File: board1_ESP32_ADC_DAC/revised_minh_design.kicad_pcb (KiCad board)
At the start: 4 copper layers, 94 x 39 mm, 31 parts, among them J1 Conn_01x03_Male, J2 Conn_01x08_Male, J3 Conn_01x08_Male, J4 Conn_01x08_Male, U1 ESP32-DevKit-C, U2 LM7805_TO220, U3 MCP1754S-3302xCB, U4 MCP1825S-3.3V, U5 MCP1501-33xSN, U6 MCP3464R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

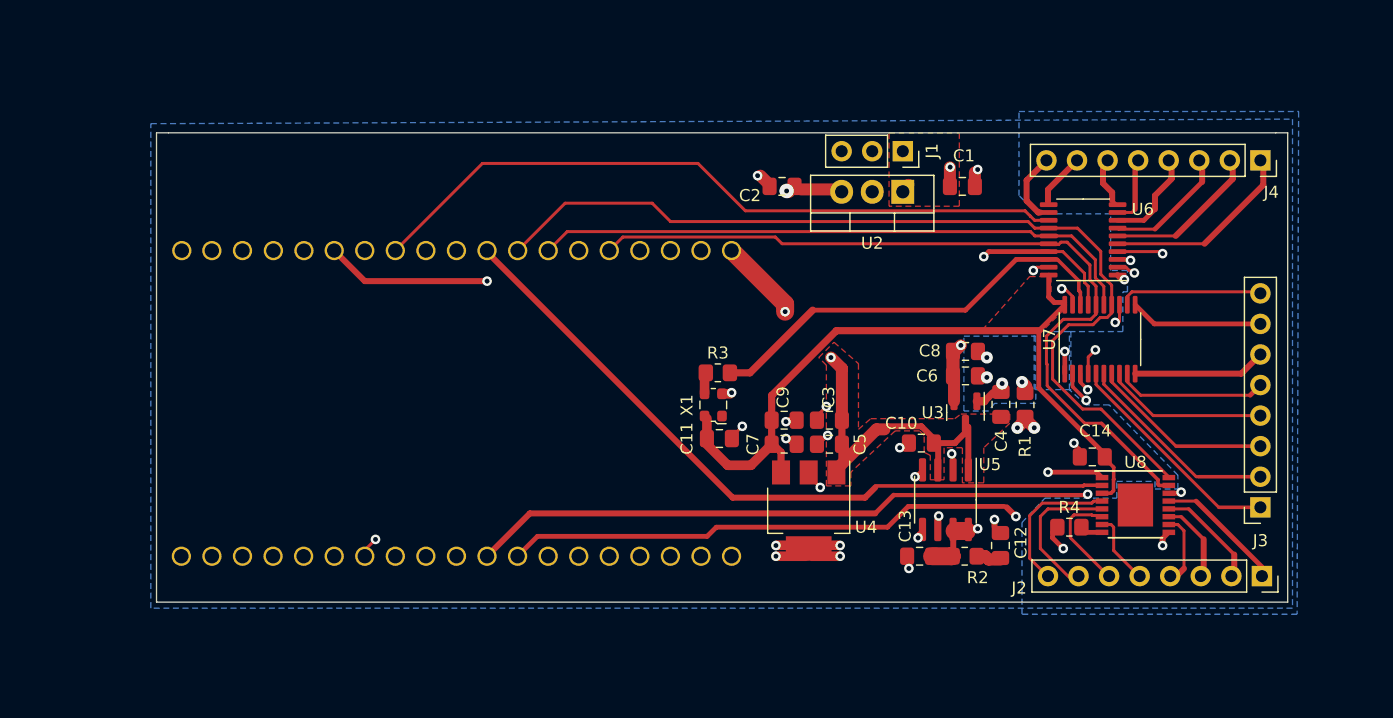
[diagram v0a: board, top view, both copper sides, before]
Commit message: Fab ready version with joined ground plane, extra caps for ADCs
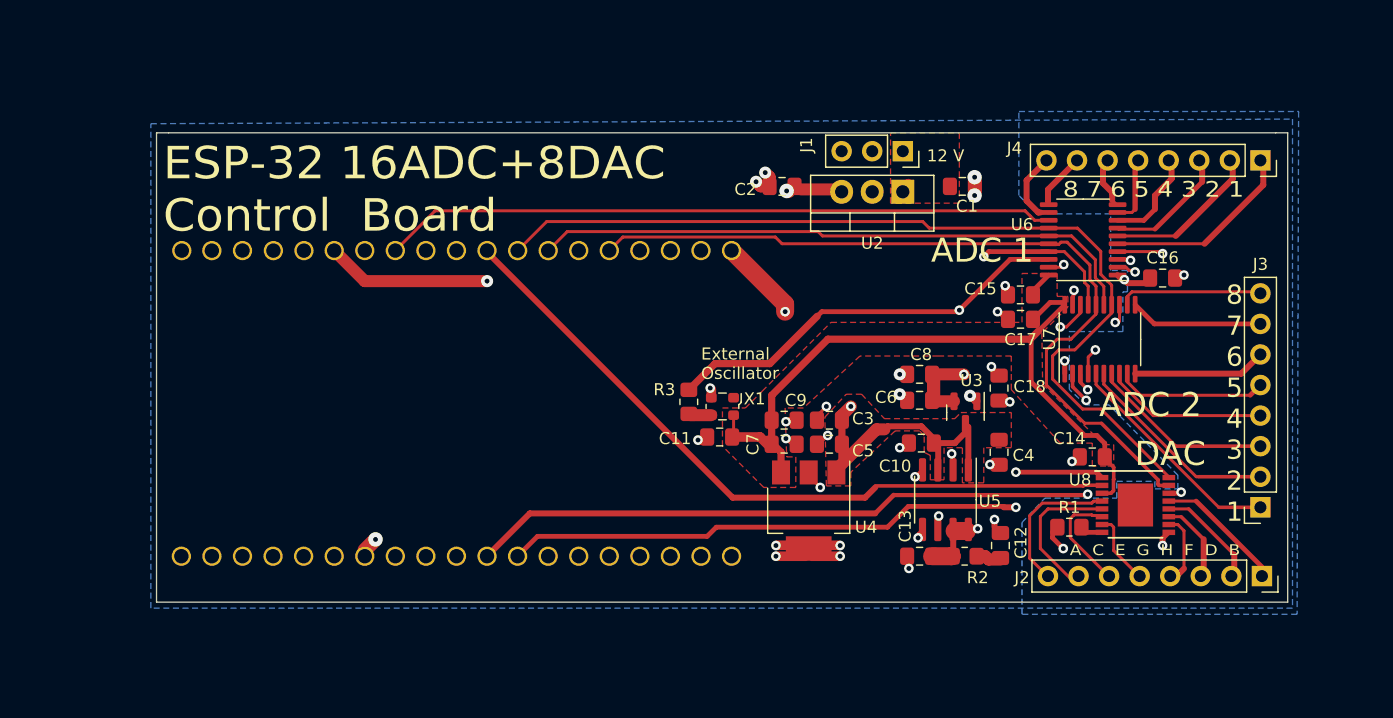
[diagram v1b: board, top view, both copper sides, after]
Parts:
- removed the R1 at (122.2, 62.6)
- added C15: 0.1uF, Capacitor_SMD:C_0805_2012Metric_Pad1.18x1.45mm_HandSolder, F.Cu at (121.8, 53.5)
- added C16: 0.1uF, Capacitor_SMD:C_0805_2012Metric_Pad1.18x1.45mm_HandSolder, F.Cu at (133.6, 52.1)
- added C17: 0.1uF, Capacitor_SMD:C_0805_2012Metric_Pad1.18x1.45mm_HandSolder, F.Cu at (121.8, 55.5)
- added C18: 0.1uF, Capacitor_SMD:C_0805_2012Metric_Pad1.18x1.45mm_HandSolder, F.Cu at (120.0, 61.2)
- moved C6 4.32 mm to (113.4, 62.2), turned to 180 degrees
- moved C8 4.26 mm to (113.4, 60.1), turned to 180 degrees
- moved C4 3.98 mm to (120.0, 66.5), turned to -90 degrees
- moved R3 3.41 mm to (94.2, 62.4), turned to 90 degrees
- moved X1 0.77 mm to (97.0, 62.7), turned to -90 degrees
- moved C11 0.13 mm to (96.8, 65.3), turned to 180 degrees
- renumbered R4 to R1
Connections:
- C4 pad 2: GNDA -> Earth
- C6 pad 2: GNDA -> Earth
- C8 pad 2: GNDA -> Earth
- U3 pad 1: GNDA -> Earth
- U6 pad 2: GNDA -> Earth
- U6 pad 3: GNDA -> Earth
- U7 pad 2: GNDA -> Earth
- U7 pad 3: GNDA -> Earth
- U8 pad 14: GNDA -> Earth
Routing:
- net GNDA: track 13.0 -> 0.00 mm, vias 9 -> 0
- net CLK: track 35.7 -> 46.6 mm, vias 0 -> 2
- net Earth: track 39.9 -> 47.8 mm, vias 26 -> 39
- net +3.3VA: track 27.2 -> 31.0 mm, vias 3 -> 4
- net ~{ADC1_CS}: track 59.2 -> 56.0 mm
- net SK: track 79.4 -> 77.4 mm
- net +12V: track 2.76 -> 1.28 mm, vias 1 -> 0
- net +5V: track 54.5 -> 53.3 mm
- net +3V3: track 63.0 -> 61.8 mm
- net LDAC: track 52.7 -> 53.4 mm
- net SO: track 68.6 -> 67.9 mm
- removed copper zone on B.Cu, net GNDA
- removed copper zone on In1.Cu, net GNDA
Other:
- board text added: "12 V"
- board text added: "8 7 6 5 4 3 2 1"
- board text added: "A C E G H F D B"
- board text added: "ADC 1"
- board text added: "ADC 2"
- board text added: "Antenna this way ->"
- board text added: "DAC"
- board text added: "ESP-32 16ADC+8DAC Control Board"
- board text added: "ESP-32 Here"
- board text added: "External Oscillator"

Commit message: Repositioned clock closer
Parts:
- moved R3 23.5 mm to (116.1, 53.7), turned to -90 degrees
- moved X1 18.5 mm to (113.4, 54.2), turned to 90 degrees
- moved C11 17.0 mm to (110.2, 54.9), turned to 90 degrees
- moved C14 0.87 mm to (126.9, 66.9)
- moved C12 0.25 mm to (120.1, 74.5)
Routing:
- net CLK: track 46.6 -> 21.6 mm
- net +3V3: track 61.8 -> 59.8 mm
- net +3.3VDAC: track 50.8 -> 49.8 mm
- added copper zone on F.Cu, net +3.3VDAC

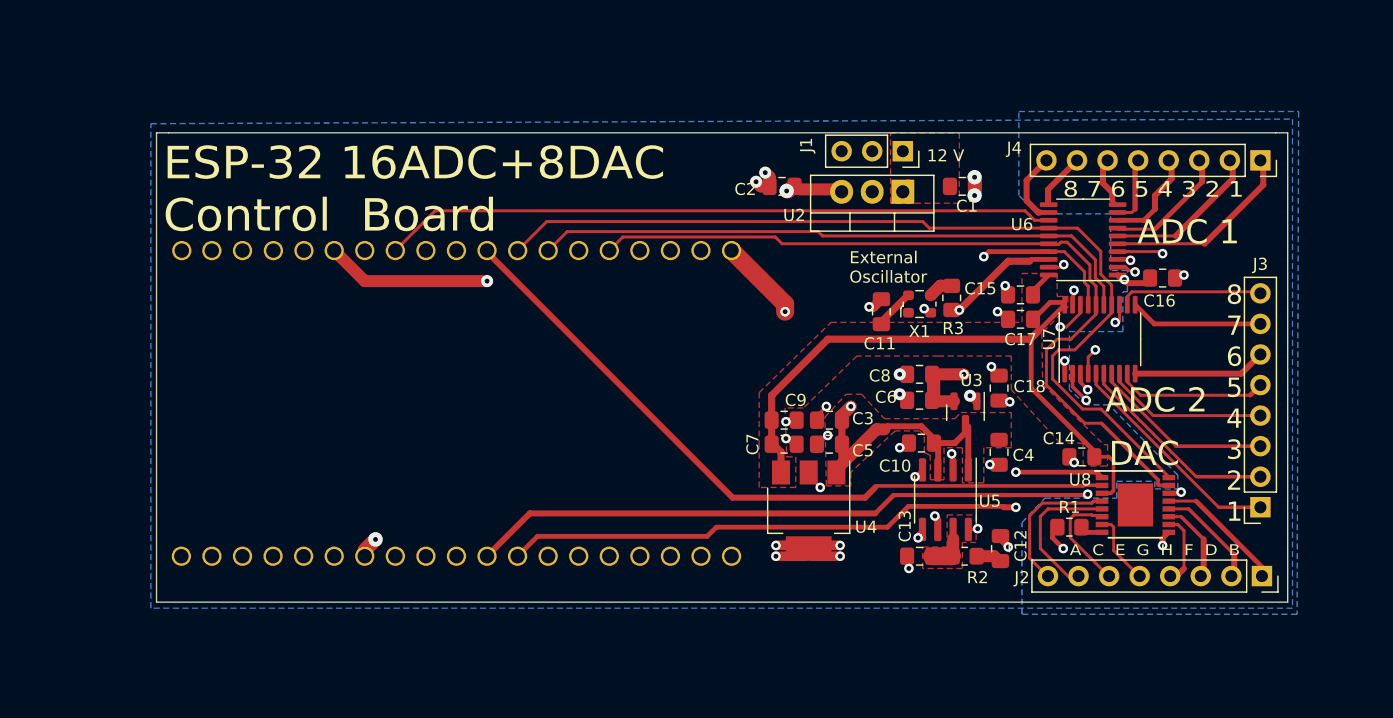
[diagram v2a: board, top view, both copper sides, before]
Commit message: JLCPB Submission. Name added, connectors changed to double layer
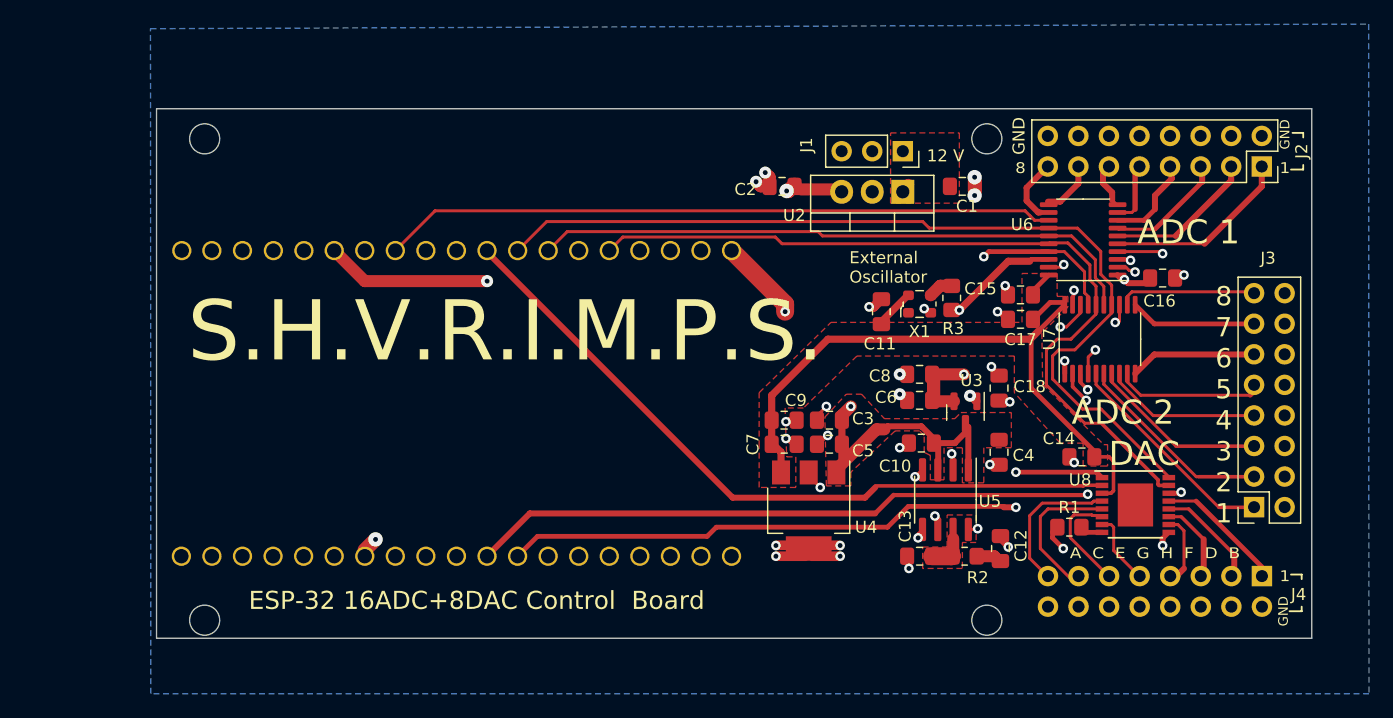
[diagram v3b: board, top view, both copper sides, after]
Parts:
- added  : MountingHole_2.5mm, MountingHole:MountingHole_2.5mm, F.Cu at (54.0, 40.5)
- added  : MountingHole_2.5mm, MountingHole:MountingHole_2.5mm, F.Cu at (119.0, 40.5)
- added  : MountingHole_2.5mm, MountingHole:MountingHole_2.5mm, F.Cu at (119.0, 80.5)
- added  : MountingHole_2.5mm, MountingHole:MountingHole_2.5mm, F.Cu at (54.0, 80.5)
- J2, J3: value Conn_01x08_Male -> Conn_02x08_Odd_Even; footprint Connector_PinSocket_2.54mm:PinSocket_1x08_P2.54mm_Vertical -> Connector_PinSocket_2.54mm:PinSocket_2x08_P2.54mm_Vertical
- J4: value Conn_01x08_Male -> Conn_02x08_Odd_Even; footprint Connector_PinSocket_2.54mm:PinSocket_1x08_P2.54mm_Vertical -> Connector_PinSocket_2.54mm:PinSocket_2x08_P2.54mm_Vertical; moved to B.Cu
- moved J4 34.5 mm to (141.9, 76.8), turned to 90 degrees
- moved J2 34.0 mm to (141.8, 42.8)
- moved J3 0.53 mm to (141.2, 71.1)
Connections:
- J2 pad 1: VoutB -> ADC1_1
- J2 pad 2: VoutD -> Earth
- J2 pad 3: VoutF -> ADC1_2
- J2 pad 4: VoutH -> Earth
- J2 pad 5: VoutG -> ADC1_3
- J2 pad 6: VoutE -> Earth
- J2 pad 7: VoutC -> ADC1_4
- J2 pad 8: VoutA -> Earth
- J3 pad 2: ADC2_2 -> Earth
- J3 pad 3: ADC2_3 -> ADC2_2
- J3 pad 4: ADC2_4 -> Earth
- J3 pad 5: ADC2_5 -> ADC2_3
- J3 pad 6: ADC2_6 -> Earth
- J3 pad 7: ADC2_7 -> ADC2_4
- J3 pad 8: ADC2_8 -> Earth
- J4 pad 1: ADC1_1 -> VoutB
- J4 pad 2: ADC1_2 -> Earth
- J4 pad 3: ADC1_3 -> VoutD
- J4 pad 4: ADC1_4 -> Earth
- J4 pad 5: ADC1_5 -> VoutF
- J4 pad 6: ADC1_6 -> Earth
- J4 pad 7: ADC1_7 -> VoutH
- J4 pad 8: ADC1_8 -> Earth
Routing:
- net ADC1_1: track 16.4 -> 15.6 mm
- net ADC1_8: track 6.61 -> 5.82 mm
- net ADC1_2: track 13.3 -> 12.5 mm
- net ADC1_4: track 8.36 -> 7.66 mm
- net ADC1_5: track 6.06 -> 5.37 mm
- net ADC1_3: track 10.7 -> 10.0 mm
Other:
- board size 94 x 39 mm -> 96 x 44 mm
- board text added: "1"
- board text added: "8"
- board text added: "GND"
- board text added: "S.H.V.R.I.M.P.S."

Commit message: JLCPB Submission. Name added, connectors changed to double layer, rounded corners
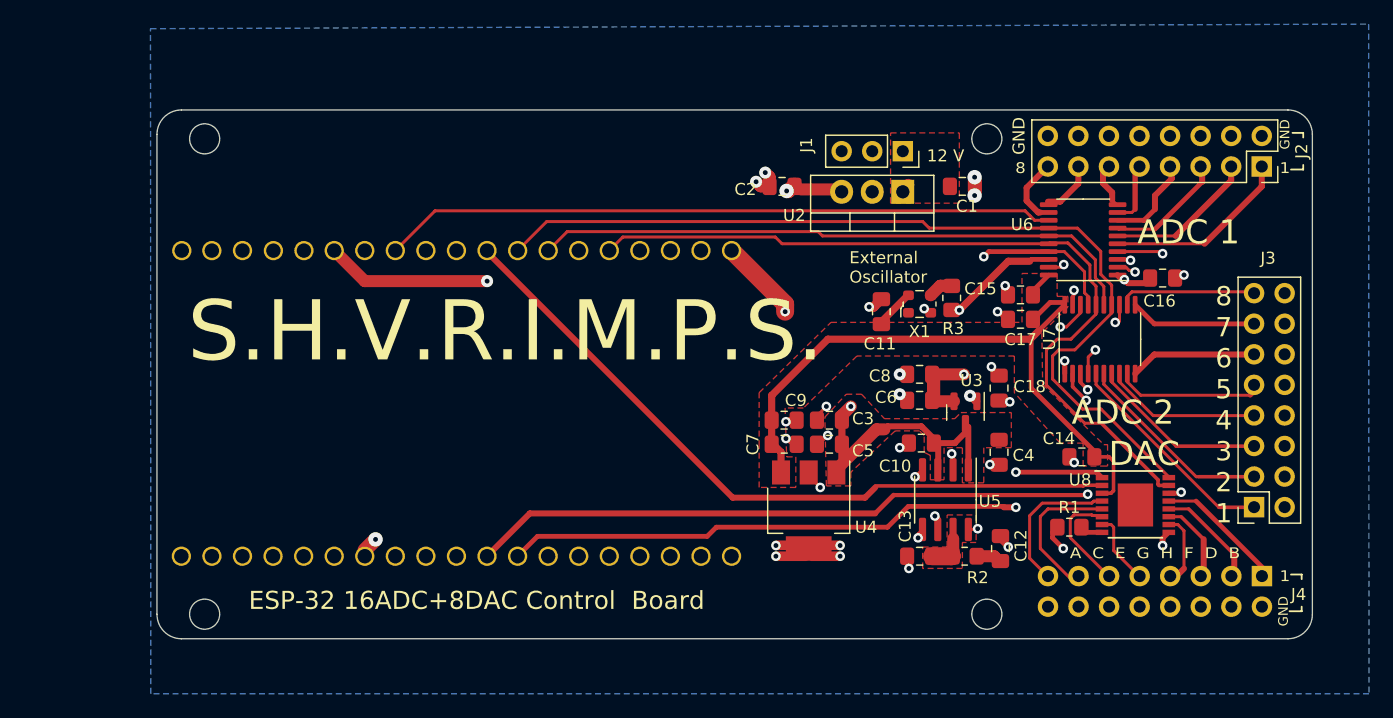
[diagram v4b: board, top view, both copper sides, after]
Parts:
- moved   0.50 mm to (119.0, 80.0)
- moved   0.50 mm to (54.0, 80.0)
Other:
- board size 96 x 44 mm -> 96 x 43.9 mm
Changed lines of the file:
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@@
       (drillshape 0)
       (scaleselection 1)
-      (outputdirectory "./")
+      (outputdirectory "Gerber/")
     )
   )
@@
   )
   (footprint "MountingHole:MountingHole_2.5mm" (layer "F.Cu")
-    (at 119 80.5)
+    (at 119 80)
     (descr "Mounting Hole 2.5mm, no annular")
     (tags "mounting hole 2.5mm no annular")
@@
   )
   (footprint "MountingHole:MountingHole_2.5mm" (layer "F.Cu")
-    (at 54 80.5)
+    (at 54 80)
     (descr "Mounting Hole 2.5mm, no annular")
     (tags "mounting hole 2.5mm no annular")
@@
   (gr_line (start 144.145 79.756) (end 145.161 79.756) (layer "F.SilkS") (width 0.15))
   (gr_line (start 144.272 76.708) (end 145.161 76.708) (layer "F.SilkS") (width 0.15))
-  (gr_line (start 146 82) (end 146 38) (layer "Edge.Cuts") (width 0.1))
-  (gr_line (start 146 38) (end 50 38) (layer "Edge.Cuts") (width 0.1))
-  (gr_line (start 50 38) (end 50 82) (layer "Edge.Cuts") (width 0.1))
-  (gr_line (start 50 82) (end 146 82) (layer "Edge.Cuts") (width 0.1))
+  (gr_arc (start 52.07 82.042) (mid 50.633159 81.446841) (end 50.038 80.01) (layer "Edge.Cuts") (width 0.1))
+  (gr_line (start 146.05 80.01) (end 146.05 40.132) (layer "Edge.Cuts") (width 0.1))
+  (gr_line (start 144.018 38.1) (end 52.07 38.1) (layer "Edge.Cuts") (width 0.1))
+  (gr_line (start 50.038 40.132) (end 50.038 80.01) (layer "Edge.Cuts") (width 0.1))
+  (gr_line (start 52.07 82.042) (end 144.018 82.042) (layer "Edge.Cuts") (width 0.1))
+  (gr_arc (start 146.05 80.01) (mid 145.454841 81.446841) (end 144.018 82.042) (layer "Edge.Cuts") (width 0.1))
+  (gr_arc (start 144.018 38.1) (mid 145.454841 38.695159) (end 146.05 40.132) (layer "Edge.Cuts") (width 0.1))
+  (gr_arc (start 50.038 40.132) (mid 50.633159 38.695159) (end 52.07 38.1) (layer "Edge.Cuts") (width 0.1))
   (gr_text "ESP-32 Here" (at 72.898 62.738) (layer "B.SilkS")
     (effects (font (size 4 4) (thickness 0.7)) (justify mirror))
